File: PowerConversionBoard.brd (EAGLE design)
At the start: 72.4 x 71.1 mm, 32 parts, among them U3 AZ1117EH-3.3TRG1

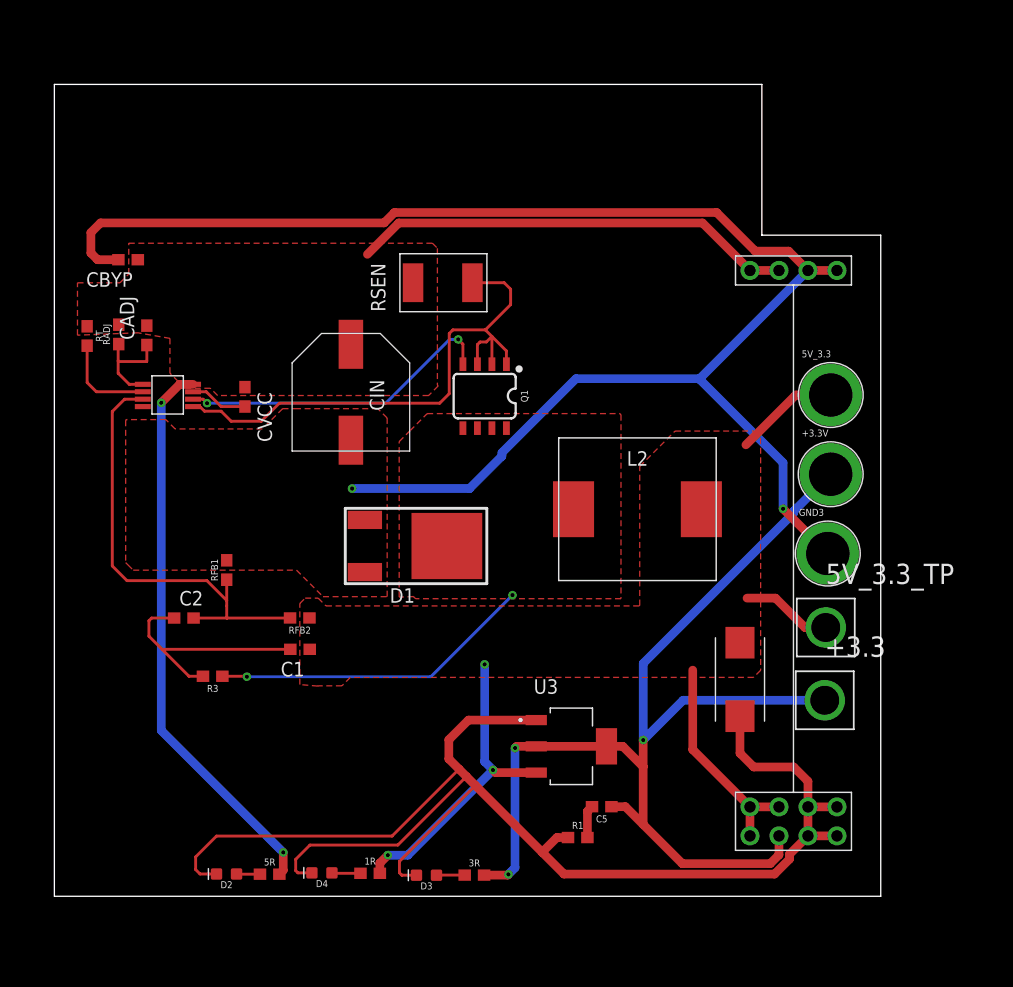
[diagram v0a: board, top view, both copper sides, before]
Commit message: Pretty much finished the layput of the board, but a few minor changes still need to be made; awaiting dimensions of potential cutoffs
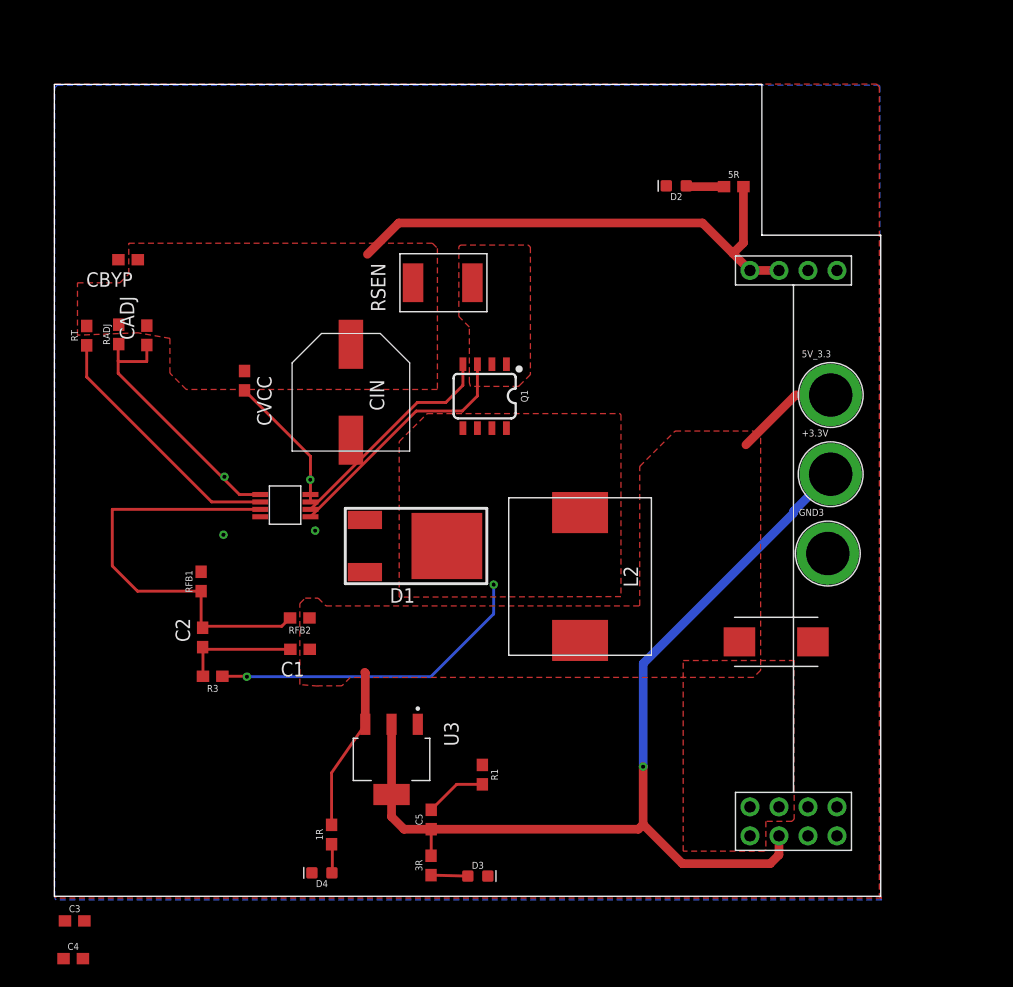
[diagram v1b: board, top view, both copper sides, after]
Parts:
- removed +3.3, 5V_3.3_TP: TP, TP:TP
- added C3, C4: 4.7uF, SparkFun-Capacitors:0603
- CIN: value 3.33uF -> 47uF
- moved 5R 72.7 mm to (59.5, 62.2)
- moved D2 72.0 mm to (54.5, 62.2)
- moved U3 15.8 mm to (29.5, 12.0), turned to 270 degrees
- moved C5 15.0 mm to (33.0, 6.73), turned to 90 degrees
- moved U$1 14.1 mm to (18.0, 33.2)
- moved R1 10.0 mm to (37.5, 10.7), turned to 270 degrees
- moved L2 7.75 mm to (46.1, 28.0), turned to 270 degrees
- moved 1R 4.79 mm to (24.3, 5.41), turned to 90 degrees
- moved COUT 4.57 mm to (63.2, 22.3), turned to 0 degrees
- moved D3 4.50 mm to (37.1, 1.77), turned to 0 degrees
- moved 3R 3.89 mm to (33.0, 2.70), turned to 90 degrees
- moved RFB1 2.46 mm to (12.9, 27.6)
- moved C2 2.37 mm to (13.0, 22.7), turned to 90 degrees
- moved CVCC 1.41 mm to (16.7, 45.2)
- turned RT to 90 degrees
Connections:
- new net RT: RT.1, U$1.2
- net +3.3V: now also C4.1; no longer +3.3.P$1
- net +48V: no longer RT.1, U$1.2
- net +5V: now also C3.1; no longer 5V_3.3_TP.P$1
- net GND: now also C3.2, C4.2
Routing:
- net GND: track 272.6 -> 0.00 mm, vias 2 -> 4
- net +48V: track 96.7 -> 45.1 mm, vias 2 -> 0
- net +5V: track 64.0 -> 23.5 mm, vias 3 -> 0
- net N$9: track 50.1 -> 21.8 mm
- net RT: track 0.00 -> 22.5 mm
- net N$1: track 9.10 -> 23.4 mm
- net +3.3V: track 99.0 -> 86.0 mm, vias 3 -> 1
- net N$11: track 21.1 -> 10.3 mm
- net N$7: track 28.0 -> 19.7 mm, vias 2 -> 0
- net N$3: track 5.08 -> 12.2 mm
- net N$12: track 2.87 -> 5.40 mm
- net N$13: track 39.7 -> 38.0 mm
- net N$4: track 2.06 -> 3.33 mm
- net N$5: track 2.48 -> 3.22 mm
- added copper zone on layer 16, net GND
- added copper zone on layer 1, net N$9

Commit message: smaller board outline
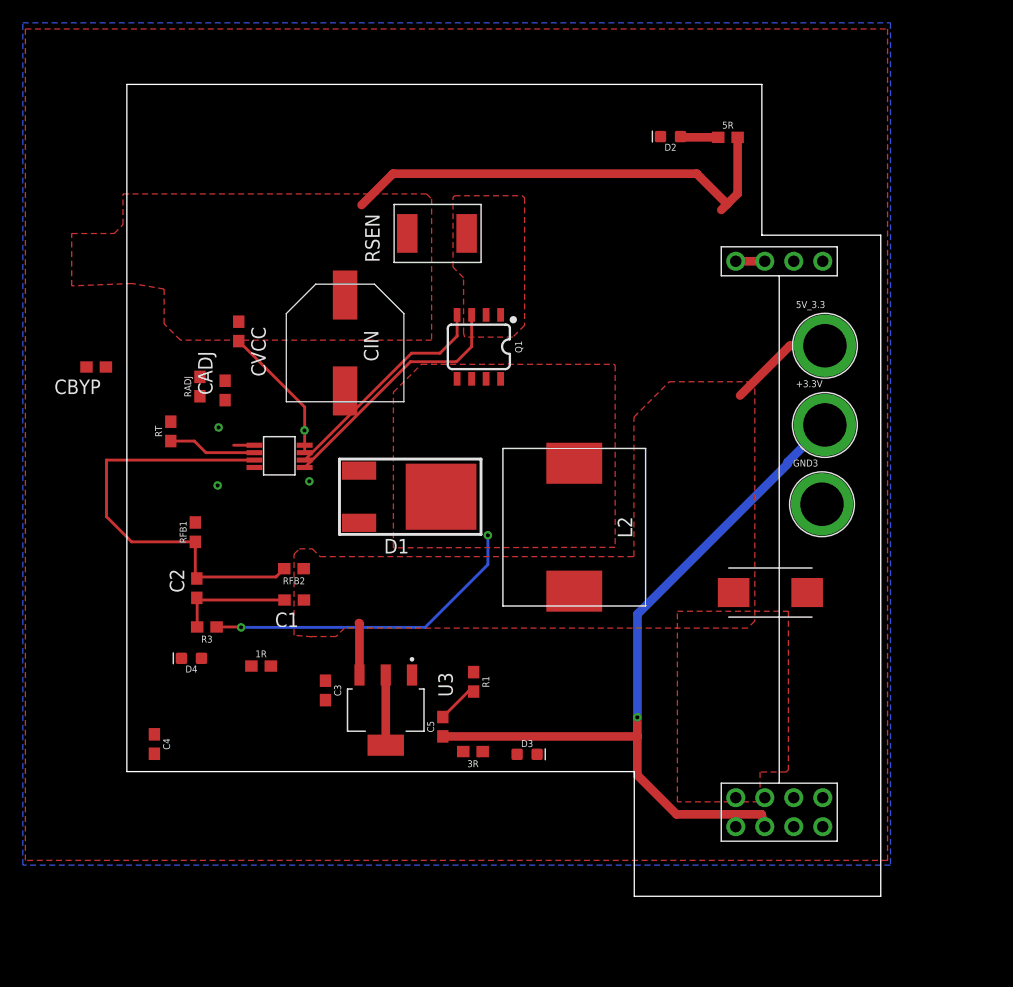
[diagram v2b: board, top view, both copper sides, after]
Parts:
- moved C3 29.8 mm to (23.7, 18.0), turned to 270 degrees
- moved D4 22.0 mm to (12.0, 20.8)
- moved C4 20.1 mm to (8.76, 13.3), turned to 270 degrees
- moved 1R 16.0 mm to (18.1, 20.2), turned to 0 degrees
- moved D3 11.5 mm to (41.4, 12.4)
- moved RT 11.2 mm to (10.2, 40.7)
- moved 3R 10.6 mm to (36.7, 12.7), turned to 180 degrees
- moved CBYP 9.80 mm to (3.66, 46.4)
- moved RADJ 8.45 mm to (12.8, 44.7)
- moved CADJ 8.39 mm to (15.0, 44.3)
- moved C5 8.19 mm to (34.0, 14.9)
- moved R1 8.16 mm to (36.7, 18.8)
- moved +3.3V 4.35 mm to (67.5, 41.3)
- moved 5R 4.35 mm to (59.0, 66.5)
- moved C1 4.35 mm to (21.0, 26.0)
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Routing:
- net N$1: track 23.4 -> 1.82 mm
- net RT: track 22.5 -> 7.75 mm
- net +3.3V: track 86.0 -> 74.1 mm
- net +5V: track 23.5 -> 13.8 mm
- net N$5: track 3.22 -> 0.47 mm
- net N$6: track 2.63 -> 0.00 mm
- net N$12: track 5.40 -> 3.63 mm
- net +48V: track 45.1 -> 43.8 mm
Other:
- board size 72.4 x 71.1 mm -> 66 x 71.1 mm

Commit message: Renamed the nets and inceased wire size where it was reasonable. Also moved around some components for strighter wiring.
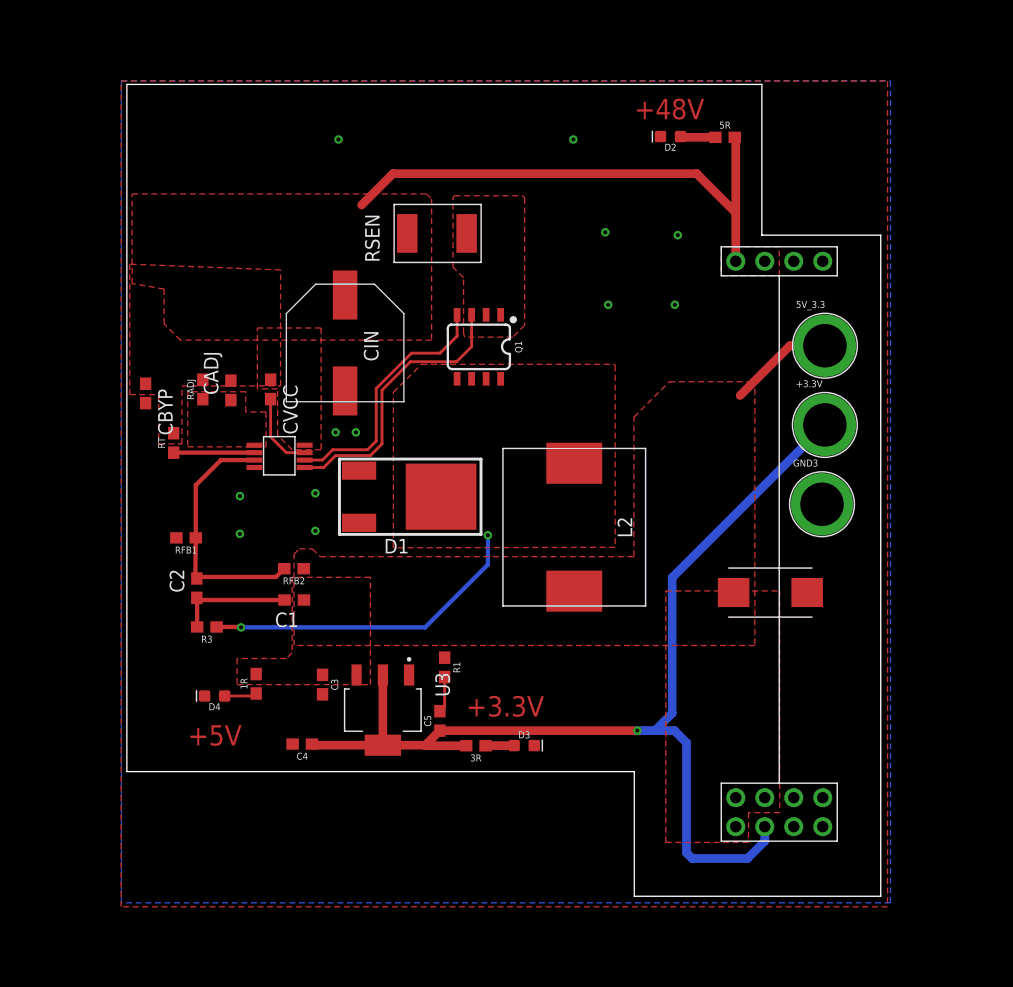
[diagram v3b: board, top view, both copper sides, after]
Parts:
- moved C4 13.0 mm to (21.7, 13.3), turned to 180 degrees
- moved CVCC 5.80 mm to (18.9, 44.4)
- moved CBYP 4.91 mm to (7.99, 44.0), turned to 270 degrees
- moved D4 3.88 mm to (14.0, 17.5)
- moved R1 2.84 mm to (34.2, 20.1)
- moved 1R 1.61 mm to (17.7, 18.6), turned to 90 degrees
- moved RT 1.05 mm to (10.5, 39.7)
- moved RFB1 0.95 mm to (11.5, 31.4), turned to 180 degrees
- moved D3 0.80 mm to (41.2, 13.2)
- moved C3 0.57 mm to (23.5, 18.5)
- moved C5 0.57 mm to (33.8, 15.4)
- moved 3R 0.57 mm to (36.9, 13.2)
- moved CADJ 0.51 mm to (15.5, 44.3)
- moved RADJ 0.36 mm to (13.0, 44.4)
- moved U3 0.25 mm to (28.8, 16.3)
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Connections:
- net N$1 renamed ADJ
- net N$10 renamed SWITCH
- net N$13 renamed FB
- net N$3 renamed VCC
- net N$7 renamed PGATE
- net N$9 renamed ISEN
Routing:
- net +3.3V: track 74.1 -> 95.1 mm
- net FB: track 38.0 -> 22.4 mm
- net VCC: track 12.2 -> 6.87 mm
- net +5V: track 13.8 -> 9.33 mm
- net N$6: track 0.00 -> 2.85 mm
- net ISEN: track 21.8 -> 24.6 mm
- net PGATE: track 19.7 -> 22.4 mm
- net N$5: track 0.47 -> 2.98 mm
- net +48V: track 43.8 -> 46.2 mm
- net ADJ: track 1.82 -> 0.00 mm
- net RT: track 7.75 -> 7.08 mm
- added copper zone on layer 1, net ADJ
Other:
- board text added: "+3.3V"
- board text added: "+48V"
- board text added: "+5V"

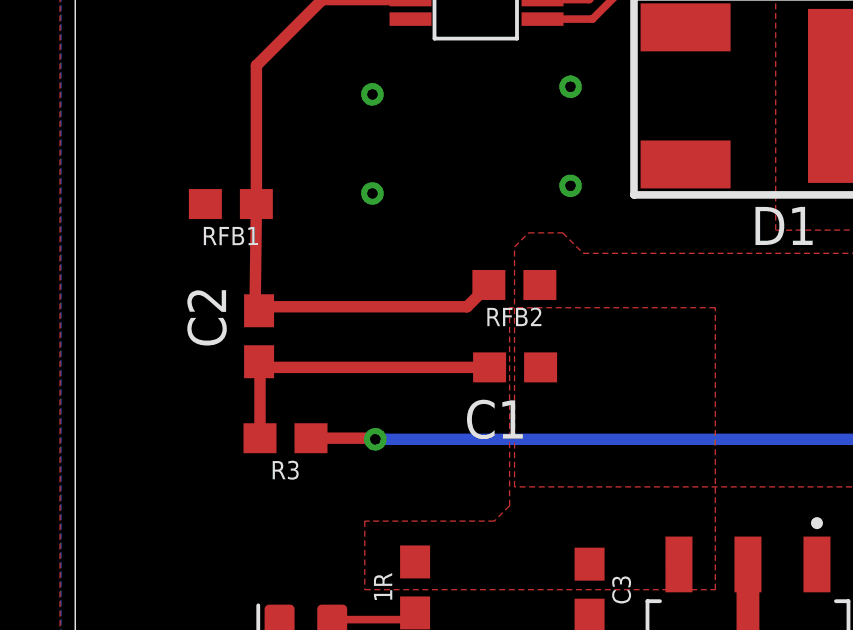
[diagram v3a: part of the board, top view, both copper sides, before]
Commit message: Renamed the nets and inceased wire size where it was reasonable. Also moved around some components for strighter wiring.
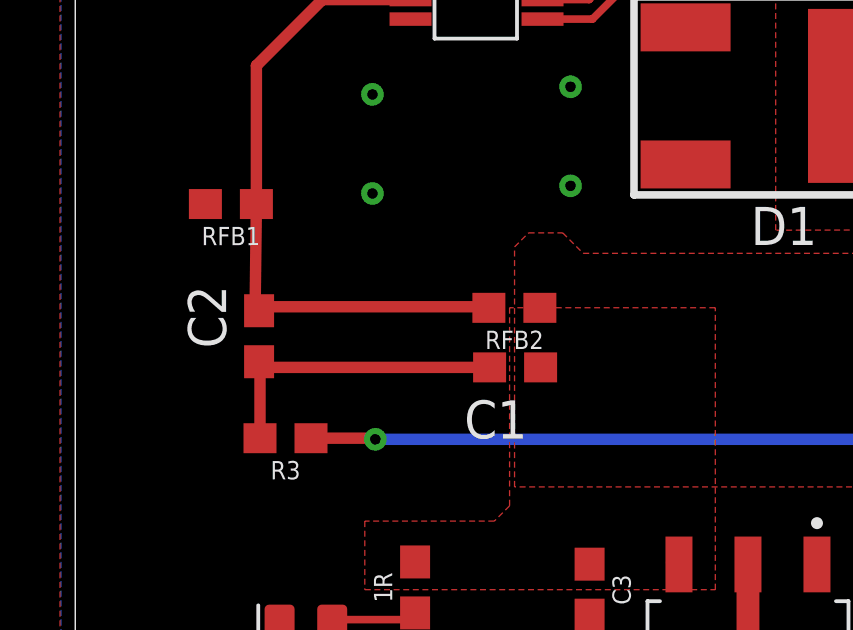
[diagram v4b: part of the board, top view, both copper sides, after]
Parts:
- moved RFB2 0.76 mm to (21.0, 27.9)
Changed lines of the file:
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@@
 <attribute name="VALUE" x="13.766709375" y="44.3969" size="0.6096" layer="27" font="vector" ratio="20" rot="R90" align="top-center"/>
 </element>
-<element name="RFB2" library="SparkFun-Resistors" library_urn="urn:adsk.eagle:library:532" package="0603" package3d_urn="urn:adsk.eagle:package:39650/1" value="15k" x="20.987596875" y="28.698421875" smashed="yes" rot="R180">
-<attribute name="NAME" x="20.987596875" y="27.936421875" size="0.6096" layer="25" font="vector" ratio="20" rot="R180" align="bottom-center"/>
-<attribute name="PROD_ID" value=" " x="20.987596875" y="28.698421875" size="1.778" layer="27" rot="R180" display="off"/>
-<attribute name="VALUE" x="20.987596875" y="29.460421875" size="0.6096" layer="27" font="vector" ratio="20" rot="R180" align="top-center"/>
+<element name="RFB2" library="SparkFun-Resistors" library_urn="urn:adsk.eagle:library:532" package="0603" package3d_urn="urn:adsk.eagle:package:39650/1" value="15k" x="20.987596875" y="27.936421875" smashed="yes" rot="R180">
+<attribute name="NAME" x="20.987596875" y="27.174421875" size="0.6096" layer="25" font="vector" ratio="20" rot="R180" align="bottom-center"/>
+<attribute name="PROD_ID" value=" " x="20.987596875" y="27.936421875" size="1.778" layer="27" rot="R180" display="off"/>
+<attribute name="VALUE" x="20.987596875" y="28.698421875" size="0.6096" layer="27" font="vector" ratio="20" rot="R180" align="top-center"/>
 </element>
 <element name="R3" library="SparkFun-Resistors" library_urn="urn:adsk.eagle:library:532" package="0603" package3d_urn="urn:adsk.eagle:package:39650/1" value="8.6k" x="13.358534375" y="23.5915625" smashed="yes" rot="R180">
@@
 <contactref element="C2" pad="2"/>
 <contactref element="U$1" pad="3"/>
-<wire x1="20.13023125" y1="28.69105625" x2="20.137596875" y2="28.698421875" width="0.254" layer="1"/>
+<wire x1="20.13023125" y1="27.92905625" x2="20.137596875" y2="27.936421875" width="0.254" layer="1"/>
 <wire x1="12.38846875" y1="31.396496875" x2="12.346496875" y2="27.9727375" width="0.381" layer="1"/>
 <wire x1="12.346496875" y1="27.9727375" x2="12.4783125" y2="27.840921875" width="0.254" layer="1"/>
-<wire x1="20.137596875" y1="28.698421875" x2="19.4119125" y2="27.9727375" width="0.381" layer="1"/>
-<wire x1="19.4119125" y1="27.9727375" x2="12.346496875" y2="27.9727375" width="0.381" layer="1"/>
+<wire x1="20.137596875" y1="27.936421875" x2="20.10128125" y2="27.9727375" width="0.381" layer="1"/>
+<wire x1="20.10128125" y1="27.9727375" x2="12.346496875" y2="27.9727375" width="0.381" layer="1"/>
 <wire x1="17.526121875" y1="38.212028125" x2="14.590028125" y2="38.212028125" width="0.381" layer="1"/>
 <wire x1="12.38846875" y1="36.01046875" x2="12.38846875" y2="31.396496875" width="0.381" layer="1"/>

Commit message: Finished the board and added the text
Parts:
- moved CBYP 12.3 mm to (19.2, 39.0), flipped to the bottom
- moved D3 7.74 mm to (37.6, 20.1), turned to 90 degrees
- moved 3R 3.74 mm to (37.6, 16.9), turned to 270 degrees
- moved C5 0.80 mm to (34.5, 15.6)
- moved R1 0.57 mm to (34.4, 19.5)
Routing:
- net +48V: track 46.2 -> 44.3 mm, vias 0 -> 1
- net N$5: track 2.98 -> 1.50 mm
- net N$12: track 3.17 -> 2.27 mm
- net +3.3V: track 95.1 -> 94.4 mm
- added copper zone on layer 1, net X
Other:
- board text added: "ROV X13 Power Conversion v1 Bryce Sasser Read Hedl, Grant Geyer 1/9/2021"

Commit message: Cleaning up git and adding exports for ordering
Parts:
- D1: device PowerComponents:DPAK-3 -> Schottky Diode 8A - MBRD835LT4G:DPAK-3
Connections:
- new net N$1: U$1.3
- net FB: no longer U$1.3
- net GND: now also D1.1, D1.3; no longer D1.P$1, D1.P$3
- net SWITCH: now also D1.4; no longer D1.P$4
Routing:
- net FB: track 22.0 -> 19.0 mm
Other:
- board text added: "ROV X13 Power Conversion v1 Bryce Sasser Read Hedl Grant Geyer 1/9/2021"
- board text removed: "ROV X13 Power Conversion v1 Bryce Sasser Read Hedl, Grant Geyer 1/9/2021"
